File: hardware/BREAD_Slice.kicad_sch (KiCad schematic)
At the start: 22 parts, among them J1 Conn_01x10_Female, J2 Screw_Terminal_01x02, J3 Screw_Terminal_01x02, J4 Screw_Terminal_01x02, J5 Screw_Terminal_01x02, U2 ACS723xMATR-10AB, U3 ACS723xMATR-10AB, U4 ACS723xMATR-10AB, U5 ACS723xMATR-10AB

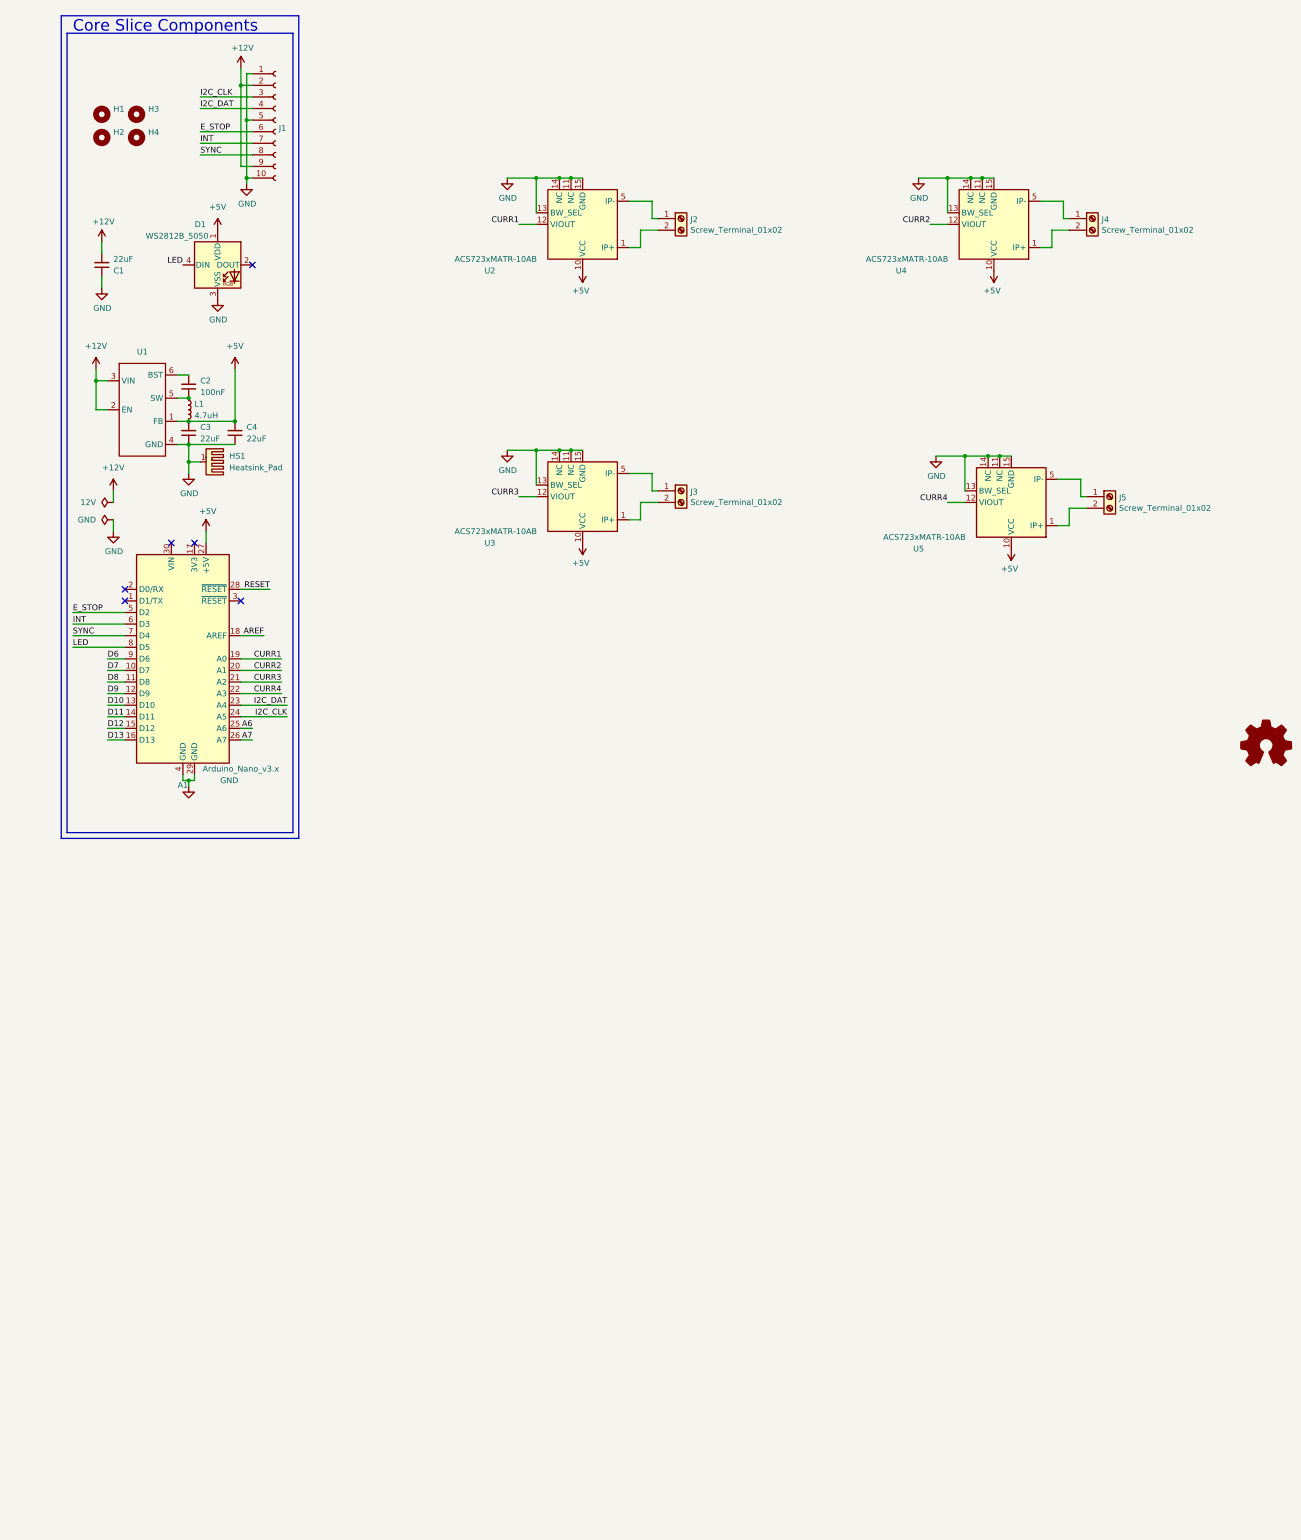
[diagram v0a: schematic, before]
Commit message: initial commit after split of ac and dc
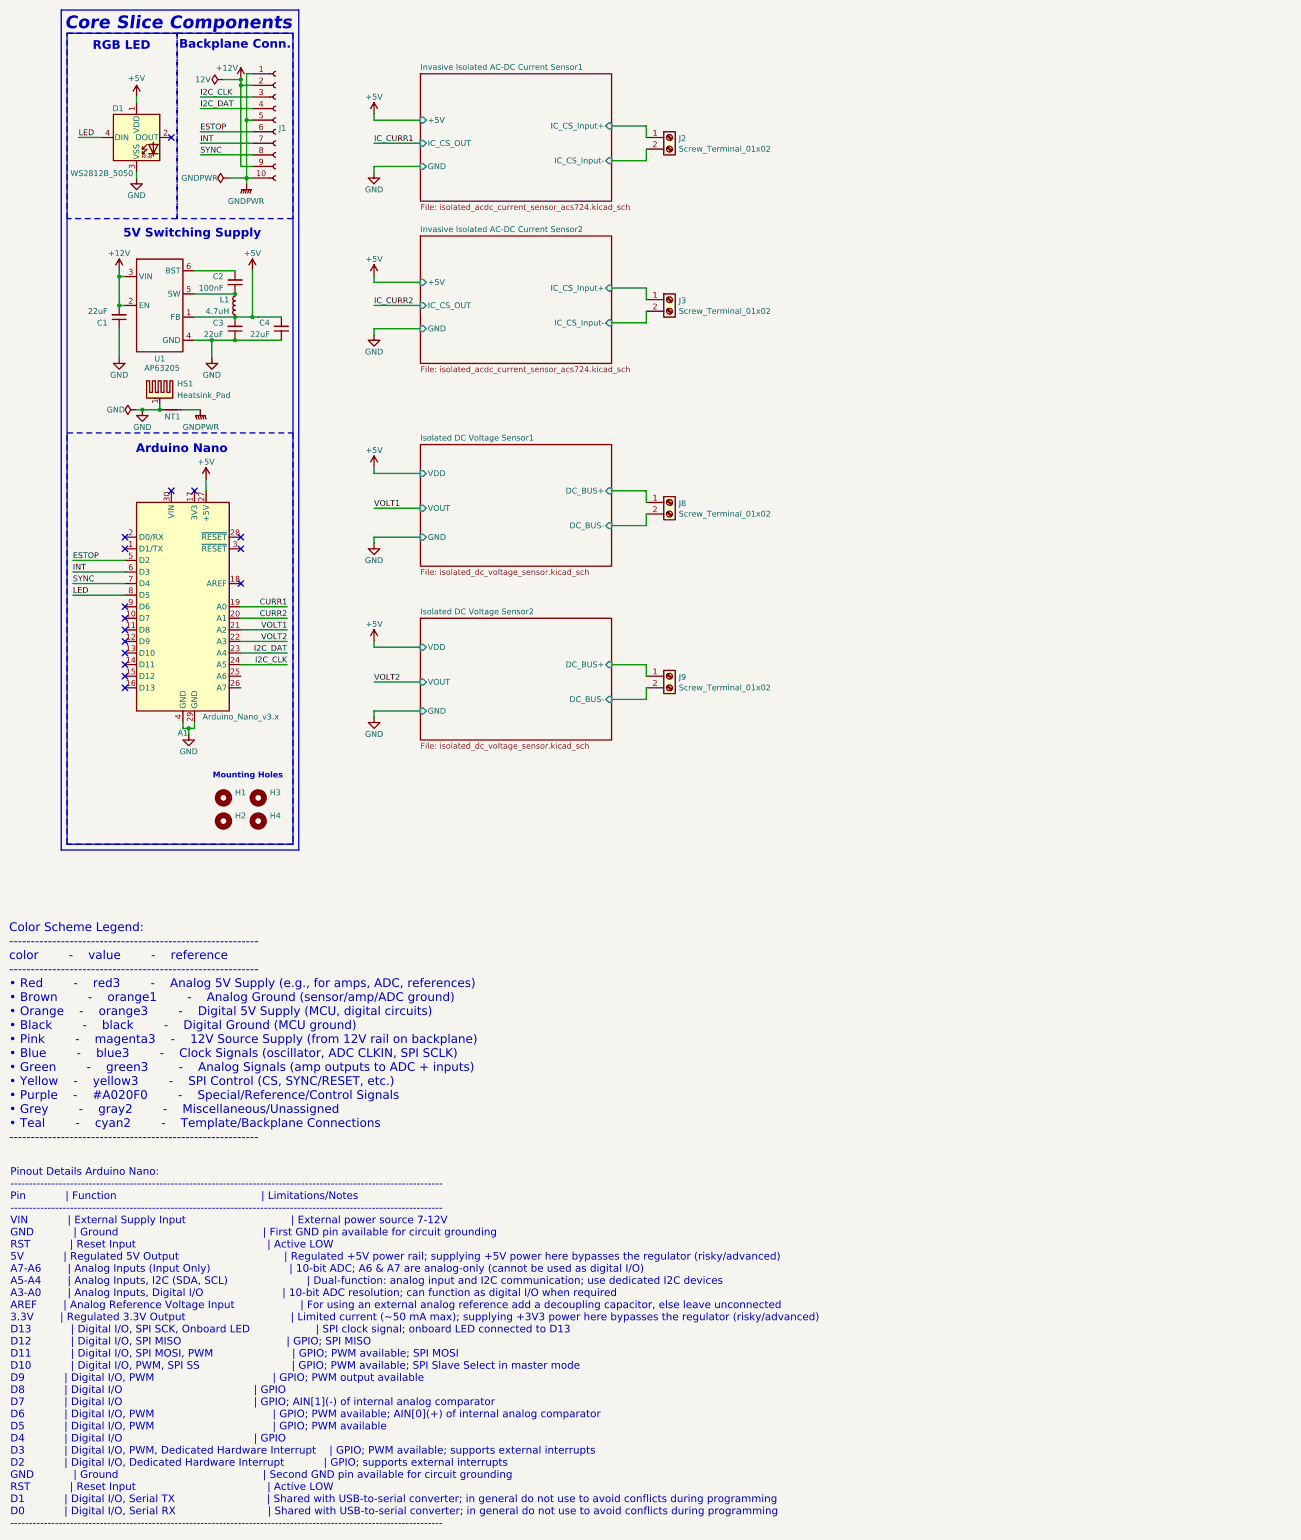
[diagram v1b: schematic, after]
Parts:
- removed J4, J5: Screw_Terminal_01x02, CRx:Pheonix Conn Term TDPT 4 2-SP-6,35-ZB, symbol Connector:Screw_Terminal_01x02
- removed U2, U3, U4, U5: ACS723xMATR-10AB, Package_SO:SOIC-16W_7.5x10.3mm_P1.27mm, symbol Sensor_Current:ACS723xMATR-10AB
- added J8, J9: Screw_Terminal_01x02, CRx:Pheonix Conn Term TDPT 4 2-SP-6,35-ZB, symbol Connector:Screw_Terminal_01x02
- added NT1: NetTie_2, NetTie:NetTie-2_SMD_Pad2.0mm, symbol Device:NetTie_2
- D1: PROD_ID (none) -> DIO-12503
- HS1: footprint KML-Custom:Thermal Pad -> kml-custom:Thermal Pad
- U1: value ~ -> AP63205
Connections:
- net GND: now also NT1.1; no longer J1.1 (Pin_1), J1.10 (Pin_10), J1.5 (Pin_5)
- net Invasive Isolated AC-DC Current Sensor1/IC_CS_Input+: now reaches J2.1 (Pin_1)
- net Invasive Isolated AC-DC Current Sensor1/IC_CS_Input-: now reaches J2.2 (Pin_2)
- net Invasive Isolated AC-DC Current Sensor2/IC_CS_Input+: now reaches J3.1 (Pin_1)
- net Invasive Isolated AC-DC Current Sensor2/IC_CS_Input-: now reaches J3.2 (Pin_2)
- net A6: no longer names the net of A1.25 (A6)
- net A7: no longer names the net of A1.26 (A7)
- net AREF: no longer names the net of A1.18 (AREF)
- net CURR3 renamed VOLT1
- net CURR4 renamed VOLT2
- net D10: no longer names the net of A1.13 (D10)
- net D11: no longer names the net of A1.14 (D11)
- net D12: no longer names the net of A1.15 (D12)
- net D13: no longer names the net of A1.16 (D13)
- net D6: no longer names the net of A1.9 (D6)
- net D7: no longer names the net of A1.10 (D7)
- net D8: no longer names the net of A1.11 (D8)
- net D9: no longer names the net of A1.12 (D9)
- net E_STOP renamed ESTOP
- net RESET: no longer names the net of A1.28 (~{RESET})
- new net GNDPWR: J1.1 (Pin_1), J1.10 (Pin_10), J1.5 (Pin_5), NT1.2
- new net Isolated DC Voltage Sensor1/DC_BUS+: J8.1 (Pin_1)
- new net Isolated DC Voltage Sensor1/DC_BUS-: J8.2 (Pin_2)
- new net Isolated DC Voltage Sensor2/DC_BUS+: J9.1 (Pin_1)
- new net Isolated DC Voltage Sensor2/DC_BUS-: J9.2 (Pin_2)
- no-connect marks 6 -> 16
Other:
- added sheet Invasive Isolated AC-DC Current Sensor1 (isolated_acdc_current_sensor_acs724.kicad_sch)
- added sheet Invasive Isolated AC-DC Current Sensor2 (isolated_acdc_current_sensor_acs724.kicad_sch)
- added sheet Isolated DC Voltage Sensor1 (isolated_dc_voltage_sensor.kicad_sch)
- added sheet Isolated DC Voltage Sensor2 (isolated_dc_voltage_sensor.kicad_sch)
- note added: "5V Switching Supply"
- note added: "Arduino Nano"
- note added: "Backplane Conn."
- note added: "Color Scheme Legend: ---------------------------------------------------------- color - value - reference ---------------------------------------------------------- • Red - red3 - Analog 5V Supply (e.g., for amps, ADC, references) • Brown - orange1 - Analog Ground (sensor/amp/ADC ground) • Orange - orange3 - Digital 5V Supply (MCU, digital circuits) • Black - black - Digital Ground (MCU ground) •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"
- note added: "Mounting Holes"
- note added: "Pinout Details Arduino Nano: -------------------------------------------------------------------------------------------------------------------- Pin | Function | Limitations/Notes -------------------------------------------------------------------------------------------------------------------- VIN | External Supply Input | External power source 7-12V GND | Ground | First GND pin available for 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"
- note added: "RGB LED"
- moved on the sheet: A1, C1, C2, C3, C4, H1, H2, H3, H4, J2, L1, U1

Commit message: completed board
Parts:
- removed J2, J3, J8, J9: Screw_Terminal_01x02, CRx:Pheonix Conn Term TDPT 4 2-SP-6,35-ZB, symbol Connector:Screw_Terminal_01x02
- added J2: 2606-1104/010-000, kml-custom:CONN4_2606-1104&slash_010-000_WAG, symbol kml-custom:WAGO_2606-1104_010-000
- D1: footprint SparkFun-LED:WS2812-5050-4PIN -> kml-custom:WS2812-5050-4PIN
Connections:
- net Invasive Isolated AC-DC Current Sensor1/IC_CS_Input+: now also J2.4
- net Invasive Isolated AC-DC Current Sensor1/IC_CS_Input-: now also J2.3
- net Isolated DC Voltage Sensor1/DC_BUS+: now also J2.1
- net Isolated DC Voltage Sensor1/DC_BUS-: now also J2.2
- net ISO_DIS: now reaches A1.9 (D6)
- net CURR2: no longer names the net of A1.20 (A1)
- net VOLT2: no longer names the net of A1.22 (A3)
- no-connect marks 16 -> 19
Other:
- removed sheet Invasive Isolated AC-DC Current Sensor2
- removed sheet Isolated DC Voltage Sensor2
- sheet Isolated DC Voltage Sensor1 ports: added ~{ISOPWR}; removed none
- note added: "HAS SPACE FOR x2 OF EACH ONCE TESTED"
